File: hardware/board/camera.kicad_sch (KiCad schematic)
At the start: 20 parts, among them CN1 AXT530124_C2924271, U26 LP3983SAB5F-08

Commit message: change of camera
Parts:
- added U27: 5054133410_C6422029, lcsc:CONN-SMD_5054133410, symbol lcsc:5054133410_C6422029
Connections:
- net CAM_CLKOUT0: now also U27.29
- net GND: now also U27.1, U27.11, U27.14, U27.17, U27.18, U27.2, U27.27, U27.28, U27.30, U27.34, U27.35, U27.36, U27.37, U27.38, U27.5, U27.8
- net I2C2_SCL_M1: now also U27.31
- net I2C2_SDA_M1: now also U27.32
- net MIPI_CSI_RX_CLK0N: now also U27.10
- net MIPI_CSI_RX_CLK0P: now also U27.9
- net MIPI_CSI_RX_D0N: now also U27.7
- net MIPI_CSI_RX_D0P: now also U27.6
- net MIPI_CSI_RX_D1N: now also U27.13
- net MIPI_CSI_RX_D1P: now also U27.12
- net MIPI_CSI_RX_D2N: now also U27.4
- net MIPI_CSI_RX_D2P: now also U27.3
- net MIPI_CSI_RX_D3N: now also U27.16
- net MIPI_CSI_RX_D3P: now also U27.15
- net MIPI_CSI_X4_RST: now also U27.26
- net VCC1V8_DOVDD_DVP: now also U27.22
- net VCC2V8_AVDD_DVP: now also U27.23
- net VCC2V8_DVP: now also U27.24
- net VDD1V2_DVDD_DVP: now also U27.21
- no-connect marks 0 -> 4

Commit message: start of ethernet
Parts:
- removed CN1: AXT530124_C2924271, lcsc:CONN-SMD_30P-P0.40_AXT530124, symbol lcsc:AXT530124_C2924271
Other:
- note added: "Close to FPC Connector"
- moved on the sheet: U27

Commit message: finished schematic!
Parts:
- added C360, C361: 100nF X5R 10V, Capacitor_SMD:C_0201_0603Metric, symbol Device:C
- added U1: RK3568, RK3568:BGA636C65P28X28_1900X1900X168, symbol RK3568:RK3568
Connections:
- net DVP_PWREN0_H_GPIO0_D3: no longer R81.2
- net GND: now also C360.2, C361.2
- net MIPI_CSI_RX_CLK0N: now also U1.AH10 (MIPI_CSI_RX_CLK0N)
- net MIPI_CSI_RX_CLK0P: now also U1.AG10 (MIPI_CSI_RX_CLK0P)
- net MIPI_CSI_RX_D0N: now also U1.AH12 (MIPI_CSI_RX_D0N)
- net MIPI_CSI_RX_D0P: now also U1.AG12 (MIPI_CSI_RX_D0P)
- net MIPI_CSI_RX_D1N: now also U1.AH11 (MIPI_CSI_RX_D1N)
- net MIPI_CSI_RX_D1P: now also U1.AG11 (MIPI_CSI_RX_D1P)
- net MIPI_CSI_RX_D2N: now also U1.AD11 (MIPI_CSI_RX_D2N)
- net MIPI_CSI_RX_D2P: now also U1.AE11 (MIPI_CSI_RX_D2P)
- net MIPI_CSI_RX_D3N: now also U1.AE9 (MIPI_CSI_RX_D3N)
- net MIPI_CSI_RX_D3P: now also U1.AD9 (MIPI_CSI_RX_D3P)
- new net MIPI_AVDD_0V9: C360.1, U1.W14 (MIPI_CSI_RX_AVDD_0V9)
- new net MIPI_AVDD_1V8: C361.1, U1.Y14 (MIPI_CSI_RX_AVDD_1V8)
- new net MIPI_CAM0_RST_L_GPIO3_C6: R81.2
- new net MIPI_CSI_RX_CLK1N: U1.AH9 (MIPI_CSI_RX_CLK1N)
- new net MIPI_CSI_RX_CLK1P: U1.AG9 (MIPI_CSI_RX_CLK1P)
- no-connect marks 4 -> 5
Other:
- note added: "Camera"
- note added: "Diff 100 Ohm ±10%"
- note added: "NEEDS REWORKING TO ANOTHER STANDARD (JETSON NANO)"
- moved on the sheet: C146, R81

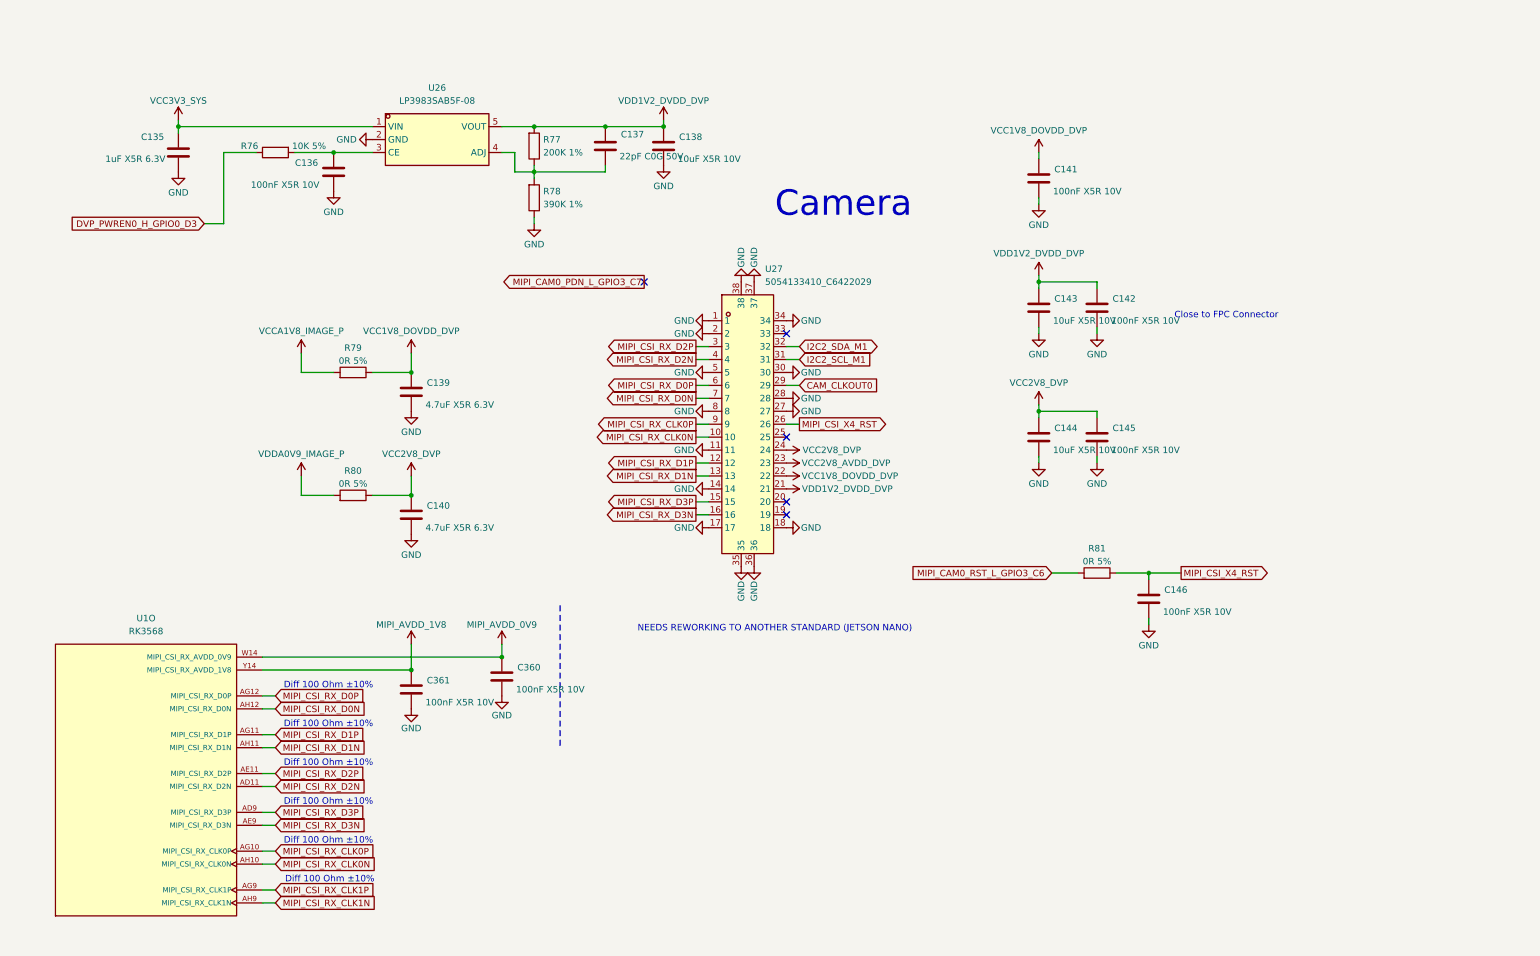
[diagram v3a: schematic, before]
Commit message: finished beautifying schematic
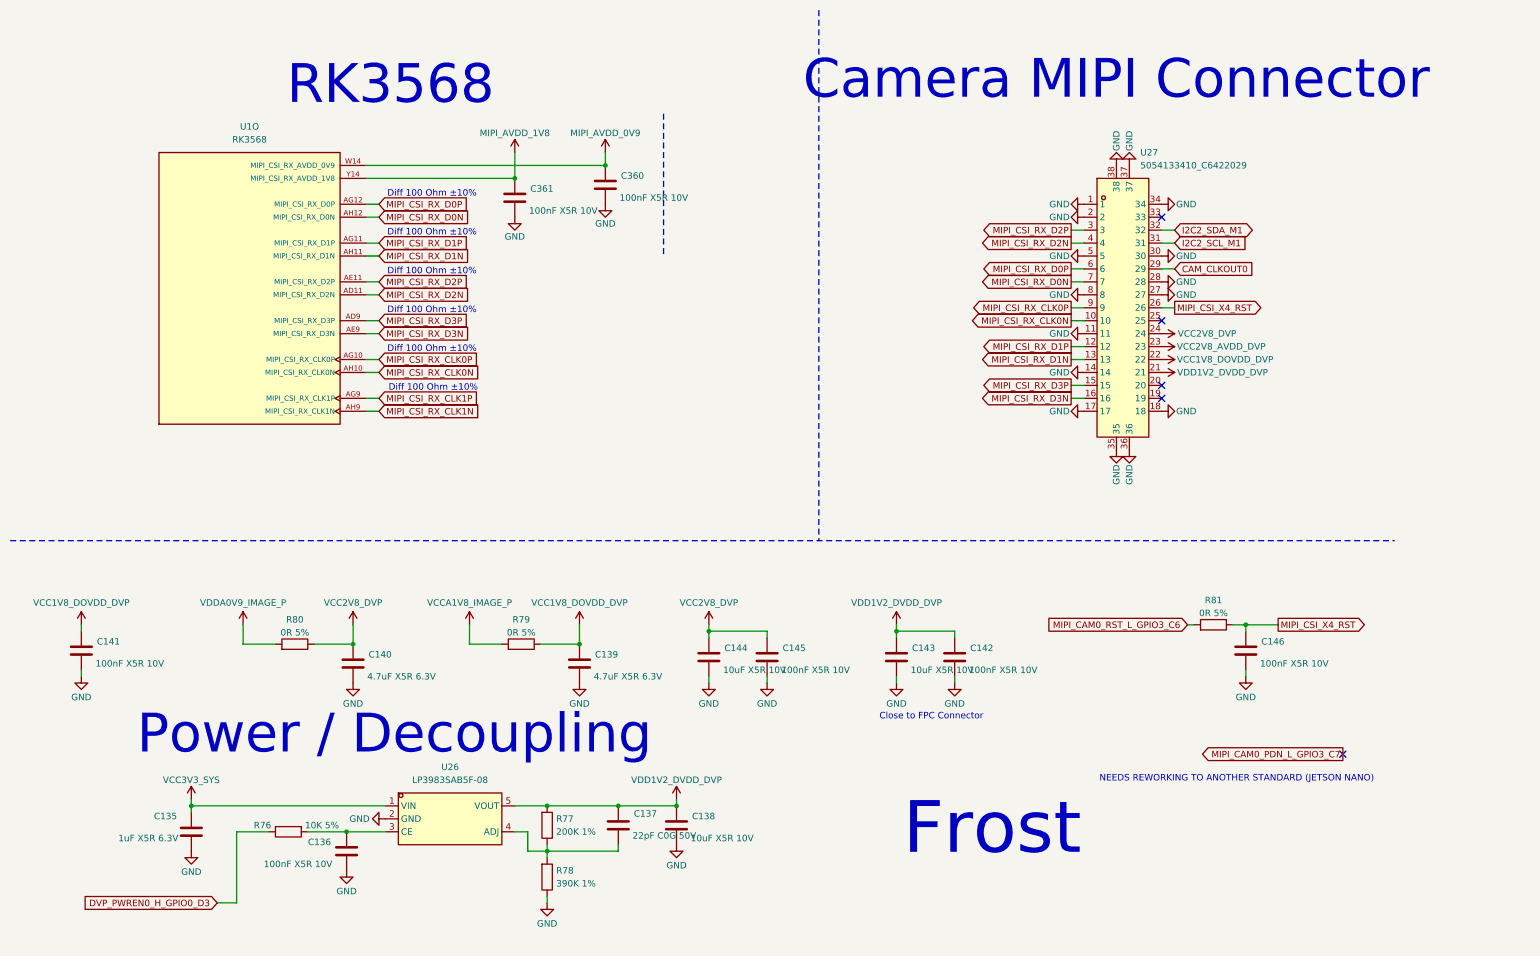
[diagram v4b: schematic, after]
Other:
- note added: "Camera MIPI Connector"
- note added: "Frost"
- note added: "Power / Decoupling"
- note added: "RK3568"
- note removed: "Camera"
- moved on the sheet: C135, C136, C137, C138, C139, C140, C141, C142, C143, C144, C145, C146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
